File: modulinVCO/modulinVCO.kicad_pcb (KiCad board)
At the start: 2 copper layers, 88.9 x 177.8 mm, 111 parts, among them J1 Conn_01x06_Pin, Q1 BC548, Q2 BC548, Q3 2N7000, Q4 BC548, Q5 BC548, SW1 SW_SPDT, U1 TL074, U2 LM7805, U3 TL074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

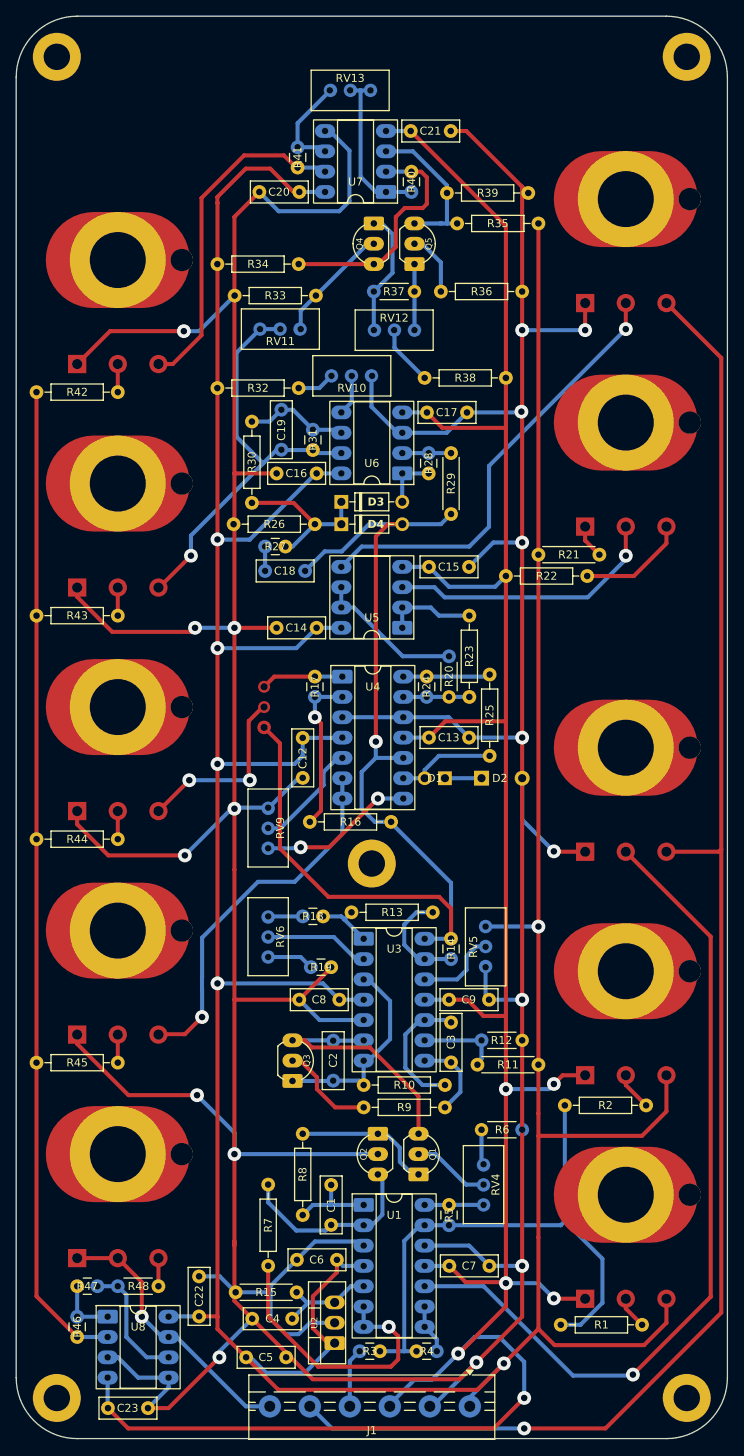
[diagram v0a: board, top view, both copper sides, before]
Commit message: Add VCF ciruit and edit for JLCPCB
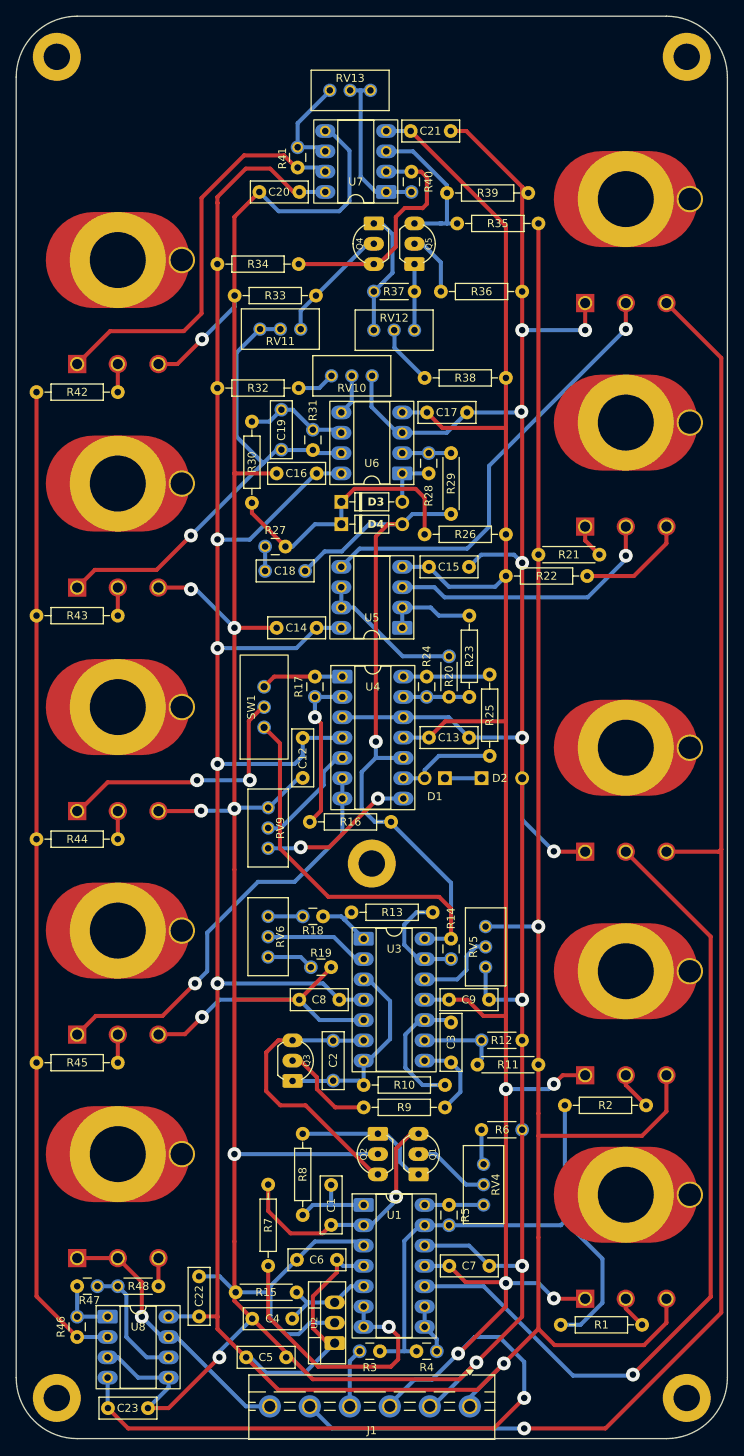
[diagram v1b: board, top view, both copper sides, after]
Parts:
- R30: value 100k 1% -> 47k
- SW1: footprint User:SW_Slide_SPST_H6.00mm_CNC -> User:SW_Slide_SPDT_H6.00mm_CNC; moved to F.Cu
- U7, U8: footprint User:DIP8_CNC -> User:DIP-8_CNC
- moved R26 34.1 mm to (86.6, 80.0), turned to 180 degrees
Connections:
- C1 pad 2: Net-(Q2-C) -> Net-(Q1-C)
- C2 pad 2: Net-(Q1-C) -> Net-(Q2-C)
- Q3 pad 1: Net-(Q1-C) -> Net-(Q2-C)
- R26 pad 1: GND -> VEE
- R7 pad 2: Net-(Q2-C) -> Net-(Q1-C)
- RV14 pad 1: /Sine -> GND
- RV14 pad 3: GND -> /Sine
- RV15 pad 1: /Triangle -> GND
- RV15 pad 3: GND -> /Triangle
- RV16 pad 1: /Sawtooth -> GND
- RV16 pad 3: GND -> /Sawtooth
- RV17 pad 1: /PWM -> GND
- RV17 pad 3: GND -> /PWM
- U1 pad 2: Net-(Q2-C) -> Net-(Q1-C)
- U3 pad 6: Net-(Q1-C) -> Net-(Q2-C)
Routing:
- net GND: track 703.4 -> 658.2 mm
- net Net-(D3-K): track 19.9 -> 34.3 mm
- net Net-(Q2-C): track 24.1 -> 36.0 mm
- net /Sawtooth: track 23.4 -> 33.3 mm
- net /Triangle: track 53.6 -> 62.2 mm
- net /Sine: track 42.5 -> 51.1 mm
- net /PWM: track 46.2 -> 53.3 mm
- net Net-(Q1-C): track 32.3 -> 32.2 mm, vias 0 -> 1
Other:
- board text added: "Invert"
- board text added: "Voltage Controlled Oscillator"

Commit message: Add STEP files
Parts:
- added C10: 100n, User:C_Radial_Polarized_P3.8mm_CNC, F.Cu at (49.0, 166.9)
- added C11: 100n, User:C_Radial_Polarized_P3.8mm_CNC, F.Cu at (86.7, 179.6)
- moved C5 1.14 mm to (58.6, 181.9)
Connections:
- RV1 pad 1: VCC -> VEE
- RV1 pad 3: VEE -> VCC
- RV2 pad 1: VCC -> VEE
- RV2 pad 3: VEE -> VCC
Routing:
- net VCC: track 506.8 -> 479.3 mm
- net VEE: track 333.6 -> 359.8 mm
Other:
- board text added: "GND"
- board text added: "LFO"
- board text added: "NOTE"
- board text added: "OUT"
- board text added: "VCC"
- board text added: "VEE"
